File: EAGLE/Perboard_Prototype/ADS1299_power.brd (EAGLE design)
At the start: 152.4 x 114.3 mm, 24 parts

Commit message: Re-wired pin 32 AGND
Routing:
- net AGND: track 297.9 -> 325.9 mm
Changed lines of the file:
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@@
 <via x="21.59" y="31.75" extent="1-16" drill="0.35"/>
 <wire x1="21.59" y1="31.75" x2="30.84" y2="50.95" width="0.1524" layer="1"/>
-<wire x1="36.84" y1="50.95" x2="52.07" y2="31.75" width="0.1524" layer="1"/>
-<wire x1="52.07" y1="31.75" x2="52.07" y2="34.29" width="0.1524" layer="1"/>
-<wire x1="52.07" y1="34.29" x2="41.91" y2="34.29" width="0.1524" layer="1"/>
+<wire x1="52.07" y1="31.75" x2="36.84" y2="50.95" width="0.1524" layer="1"/>
 <via x="41.91" y="34.29" extent="1-16" drill="0.35"/>
+<wire x1="24.13" y1="24.13" x2="24.13" y2="21.59" width="0.1524" layer="1"/>
+<wire x1="24.13" y1="21.59" x2="52.07" y2="21.59" width="0.1524" layer="1"/>
+<wire x1="52.07" y1="21.59" x2="52.07" y2="31.75" width="0.1524" layer="1"/>
 </signal>
 <signal name="+5V">

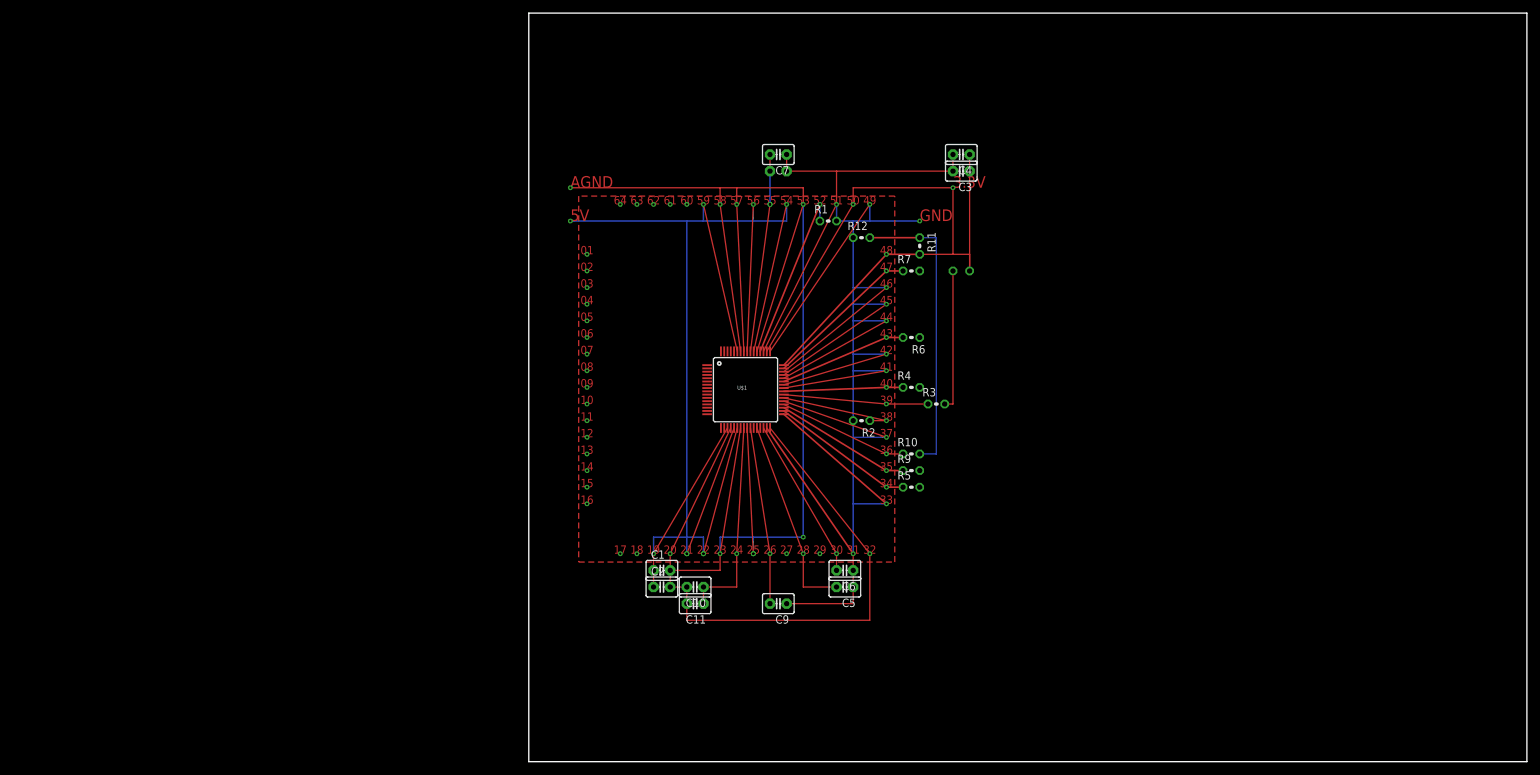
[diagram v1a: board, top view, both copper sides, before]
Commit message: Re-routed all sides and placed components on top
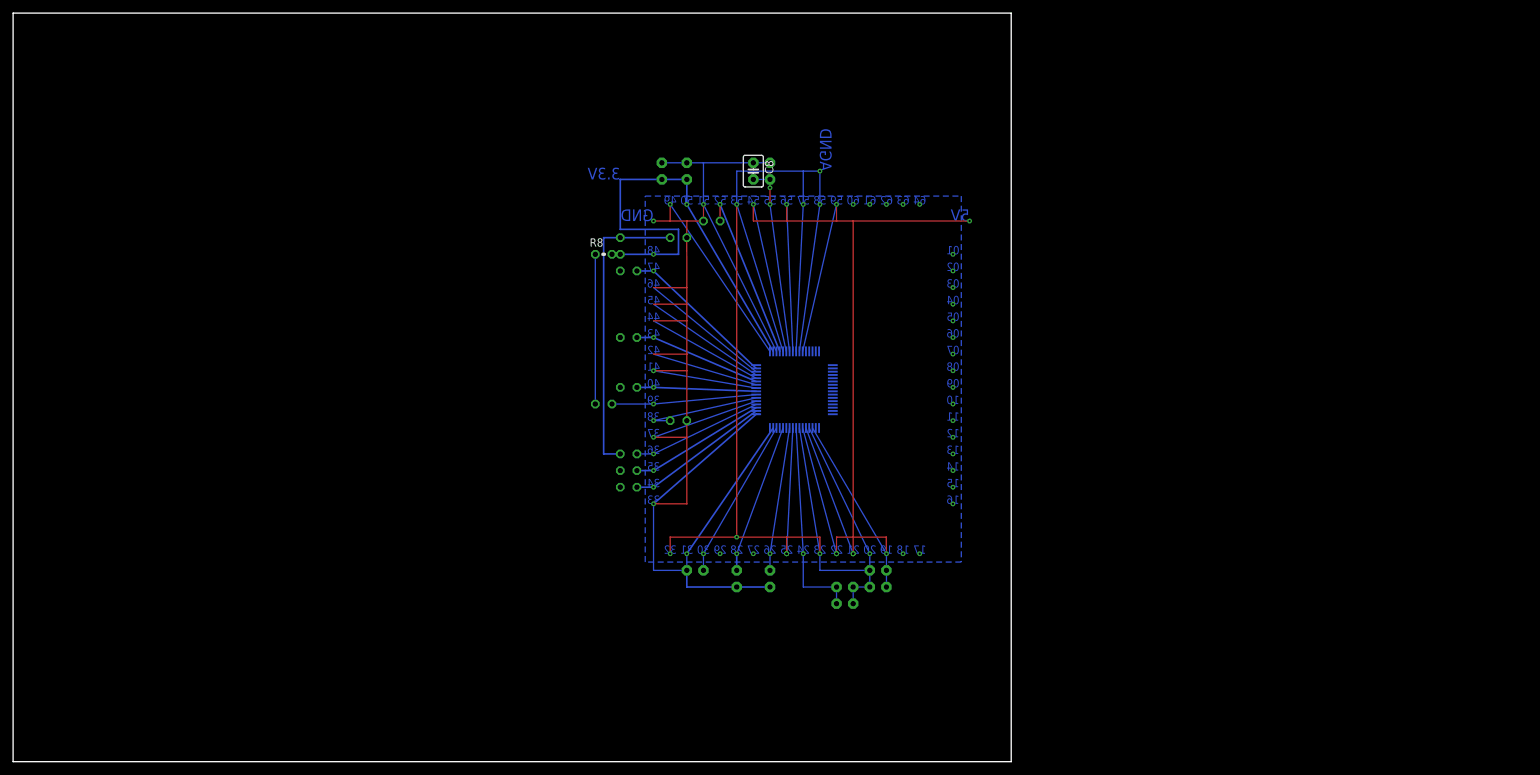
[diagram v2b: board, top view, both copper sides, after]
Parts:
- C1, C4, C6, C7, C9: value (none) -> 1uF
- C10: value (none) -> 10uF
- C11, C2, C3, C8: value (none) -> 0.1uF
- C5: value (none) -> 100uF
- R1: value (none) -> 21K
- R12: value (none) -> 22k
- R2: value (none) -> 21k
- moved R8 54.7 mm to (11.4, 77.5), flipped to the top, turned to 0 degrees
- moved R3 50.8 mm to (11.4, 54.6), flipped to the bottom
- moved C4 45.8 mm to (20.3, 90.2), flipped to the bottom, turned to 90 degrees
- moved R11 45.7 mm to (14.0, 78.7), flipped to the bottom
- moved R10 43.2 mm to (15.2, 47.0), flipped to the bottom
- moved R4 43.2 mm to (15.2, 57.1), flipped to the bottom
- moved R5 43.2 mm to (15.2, 41.9), flipped to the bottom
- moved R6 43.2 mm to (15.2, 64.8), flipped to the bottom
- moved R7 43.2 mm to (15.2, 74.9), flipped to the bottom
- moved R9 43.2 mm to (15.2, 44.5), flipped to the bottom
- moved C3 41.9 mm to (24.1, 90.2), flipped to the bottom, turned to 90 degrees
- moved C1 33.0 mm to (53.3, 29.2), flipped to the bottom
- moved C2 33.0 mm to (53.3, 26.7), flipped to the bottom
- moved R12 27.9 mm to (22.9, 80.0), flipped to the bottom
- moved R2 27.9 mm to (22.9, 52.1), flipped to the bottom
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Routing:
- net AGND: track 325.9 -> 258.2 mm
- net +3V3: track 110.1 -> 70.5 mm, vias 1 -> 0
- net GND: track 360.4 -> 350.5 mm
- net N$6: track 30.6 -> 23.0 mm
- net N$1: track 27.1 -> 22.0 mm
- net N$13: track 21.6 -> 22.9 mm
- net N$2: track 30.3 -> 29.0 mm, vias 1 -> 2
- added copper zone on layer 16, net N$5
- removed copper zone on layer 1, net N$5

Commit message: updated schematic and board
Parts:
- R2: value 21k -> 22k
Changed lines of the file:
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@@
 <element name="R11" library="resistor" library_urn="urn:adsk.eagle:library:348" package="0204V" package3d_urn="urn:adsk.eagle:package:25948/1" value="" x="13.97" y="78.74" rot="MR270"/>
 <element name="R12" library="resistor" library_urn="urn:adsk.eagle:library:348" package="0204V" package3d_urn="urn:adsk.eagle:package:25948/1" value="22k" x="22.86" y="80.01" rot="MR0"/>
-<element name="R2" library="resistor" library_urn="urn:adsk.eagle:library:348" package="0204V" package3d_urn="urn:adsk.eagle:package:25948/1" value="21k" x="22.86" y="52.07" rot="MR180"/>
+<element name="R2" library="resistor" library_urn="urn:adsk.eagle:library:348" package="0204V" package3d_urn="urn:adsk.eagle:package:25948/1" value="22k" x="22.86" y="52.07" rot="MR180"/>
 <element name="R3" library="resistor" library_urn="urn:adsk.eagle:library:348" package="0204V" package3d_urn="urn:adsk.eagle:package:25948/1" value="" x="11.43" y="54.61" rot="MR0"/>
 <element name="R4" library="resistor" library_urn="urn:adsk.eagle:library:348" package="0204V" package3d_urn="urn:adsk.eagle:package:25948/1" value="" x="15.24" y="57.15" rot="MR0"/>
@@
 <wire x1="41.82" y1="62.65" x2="46.99" y2="85.09" width="0.1524" layer="16"/>
 <wire x1="46.99" y1="85.09" x2="46.99" y2="82.55" width="0.1524" layer="1"/>
-<wire x1="49.496959375" y1="82.55" x2="46.99" y2="82.55" width="0.1524" layer="1"/>
-<wire x1="49.53" y1="82.55" x2="67.31" y2="82.55" width="0.1524" layer="1"/>
+<wire x1="46.99" y1="82.55" x2="67.31" y2="82.55" width="0.1524" layer="1"/>
 <wire x1="40.32" y1="62.65" x2="39.37" y2="85.09" width="0.1524" layer="16"/>
 <wire x1="46.99" y1="82.55" x2="39.37" y2="82.55" width="0.1524" layer="1"/>
@@
 <wire x1="42.32" y1="50.95" x2="49.53" y2="31.75" width="0.1524" layer="16"/>
 <via x="49.53" y="31.75" extent="1-16" drill="0.35"/>
-<wire x1="49.53" y1="31.75" x2="49.53" y2="34.29" width="0.1524" layer="1"/>
+<wire x1="49.53" y1="31.75" x2="46.99" y2="34.29" width="0" layer="19" extent="1-16"/>
+<wire x1="46.99" y1="34.29" x2="49.53" y2="34.29" width="0.1524" layer="1"/>
 <wire x1="49.53" y1="34.29" x2="54.61" y2="34.29" width="0.1524" layer="1"/>
 <wire x1="54.61" y1="34.29" x2="54.61" y2="31.75" width="0.1524" layer="1"/>
@@
 <via x="46.99" y="31.75" extent="1-16" drill="0.35"/>
 <wire x1="46.99" y1="31.75" x2="46.99" y2="34.29" width="0.1524" layer="1"/>
-<wire x1="46.99" y1="34.29" x2="49.53" y2="34.29" width="0.1524" layer="1"/>
 <wire x1="54.61" y1="29.21" x2="54.61" y2="26.67" width="0.1524" layer="16"/>
-<wire x1="49.53" y1="34.29" x2="49.53" y2="82.55" width="0.1524" layer="1"/>
-<wire x1="49.53" y1="82.55" x2="49.496959375" y2="82.55" width="0.1524" layer="1"/>
+<wire x1="46.99" y1="34.29" x2="46.99" y2="82.55" width="0.1524" layer="1"/>
+<wire x1="49.53" y1="34.29" x2="49.53" y2="31.75" width="0.1524" layer="1"/>
+<wire x1="46.99" y1="85.09" x2="46.99" y2="85.09" width="0" layer="19" extent="1-16"/>
 <wire x1="39.37" y1="85.09" x2="39.37" y2="85.09" width="0" layer="19" extent="1-16"/>
 <wire x1="34.29" y1="85.09" x2="34.29" y2="85.09" width="0" layer="19" extent="1-16"/>
-<wire x1="46.99" y1="85.09" x2="46.99" y2="85.09" width="0" layer="19" extent="1-16"/>
 <wire x1="54.61" y1="31.75" x2="54.61" y2="31.75" width="0" layer="19" extent="1-16"/>
 </signal>
